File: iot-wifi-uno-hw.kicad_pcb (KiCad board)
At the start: 2 copper layers, 68.6 x 53.3 mm, 86 parts, among them CON1 BARREL_JACK, P1 CONN_01X08, P2 CONN_01X08, P3 CONN_01X06, P4 CONN_01X10, P5 CONN_01X04, Q1 Q_NPN_CBE, Q2 Q_NPN_CBE, U1 usb_mini_b, U2 BD00GA5WEFJ, U3 MCP16311-MNY, U4 CH340G, U5 ESP-12E, U6 MCP6001R, U7 MOSFET-P, X1 CRYSTAL_ABM3C

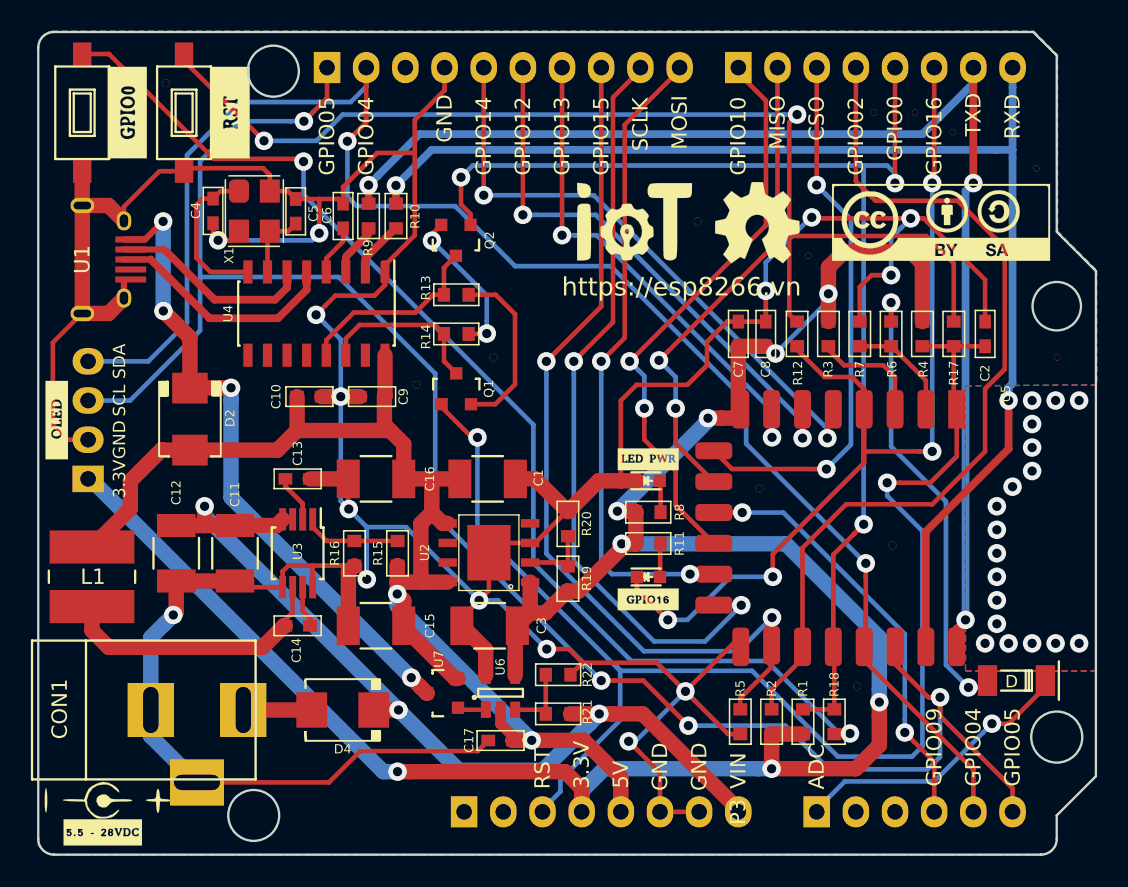
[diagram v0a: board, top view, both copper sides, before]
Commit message: Fix PCB diode zenner right
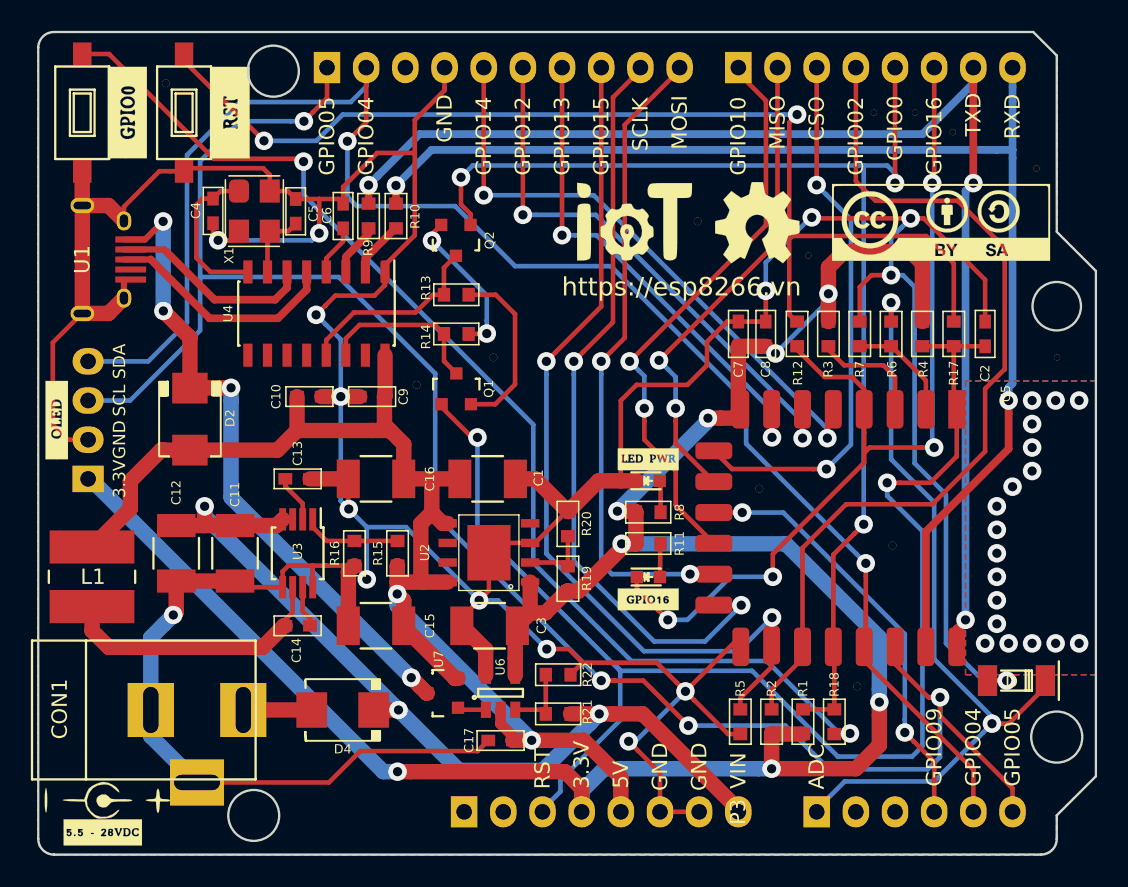
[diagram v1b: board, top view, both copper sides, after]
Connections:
- D pad 2: ADC_EX -> GND
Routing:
- net GND: track 293.4 -> 325.4 mm, vias 15 -> 16
- net ADC_EX: track 48.4 -> 49.9 mm, vias 3 -> 2
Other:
- net class Default: trace_width 0.5 -> 0.3
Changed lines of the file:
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@@
     (links 165)
     (no_connects 4)
-    (area 109.471337 58.578471 178.201339 112.068473)
+    (area 101.163667 55.951666 178.338002 114.228333)
     (thickness 1.6)
     (drawings 48)
-    (tracks 821)
+    (tracks 828)
     (zones 0)
     (modules 86)
@@
   )
   (setup
-    (last_trace_width 0.5)
+    (last_trace_width 0.3)
     (trace_clearance 0.1)
     (zone_clearance 0.5)
@@
     (mod_text_size 1 1)
     (mod_text_width 0.25)
-    (pad_size 0.4 0.4)
-    (pad_drill 0.4)
+    (pad_size 1.25 2)
+    (pad_drill 0)
     (pad_to_mask_clearance 0.2)
     (aux_axis_origin 0 0)
@@
   (net_class Default "This is the default net class."
     (clearance 0.1)
-    (trace_width 0.5)
+    (trace_width 0.3)
     (via_dia 1.2)
     (via_drill 0.6)
@@
       (net 9 ADC_EX))
     (pad 2 smd rect (at 1.875 0 180) (size 1.25 2) (layers F.Cu F.Paste F.Mask)
-      (net 9 ADC_EX))
+      (net 44 GND))
     (model "/home/trinhduc/Desktop/kicadlibrary/Untitled Folder/walter/smd_diode/sod80c.wrl"
       (at (xyz 0 0 0))
@@
   (via (at 157.124402 96.6216) (size 1.2) (drill 0.6) (layers F.Cu B.Cu) (net 8))
   (segment (start 157.1 97.82) (end 157.1 99.5162) (width 0.3) (layer F.Cu) (net 8) (status 30))
-  (segment (start 164.846 76.2) (end 164.846 85.5345) (width 0.3) (layer B.Cu) (net 9))
-  (segment (start 164.846 85.5345) (end 168.402 89.0905) (width 0.3) (layer B.Cu) (net 9))
-  (segment (start 168.402 89.0905) (end 168.402 99.695) (width 0.3) (layer B.Cu) (net 9))
-  (segment (start 168.402 99.695) (end 169.8625 101.1555) (width 0.3) (layer B.Cu) (net 9))
+  (segment (start 164.846 76.2) (end 164.846 86.36) (width 0.3) (layer B.Cu) (net 9))
+  (segment (start 164.846 86.36) (end 167.64 89.154) (width 0.3) (layer B.Cu) (net 9))
+  (segment (start 167.64 89.154) (end 167.64 99.314) (width 0.3) (layer B.Cu) (net 9))
+  (segment (start 167.64 99.314) (end 171.3865 103.0605) (width 0.3) (layer B.Cu) (net 9))
+  (segment (start 171.3865 103.0605) (end 171.3865 103.505) (width 0.3) (layer B.Cu) (net 9))
   (segment (start 160.02 109.22) (end 160.02 109.0676) (width 0.3) (layer B.Cu) (net 9))
   (segment (start 160.02 109.0676) (end 161.8361 107.2515) (width 0.3) (layer B.Cu) (net 9))
@@
   (segment (start 174.849 101.122) (end 174.849 100.711) (width 0.3) (layer F.Cu) (net 9))
   (via (at 171.3865 103.505) (size 1.2) (drill 0.6) (layers F.Cu B.Cu) (net 9))
-  (segment (start 169.8625 101.1555) (end 170.6545 101.1555) (width 0.3) (layer F.Cu) (net 9))
-  (segment (start 170.6545 101.1555) (end 171.099 100.711) (width 0.3) (layer F.Cu) (net 9))
-  (via (at 169.8625 101.1555) (size 1.2) (drill 0.6) (layers F.Cu B.Cu) (net 9))
   (segment (start 164.846 77.432001) (end 164.846 76.2) (width 0.3) (layer F.Cu) (net 9))
   (via (at 164.846 76.2) (size 1.2) (drill 0.6) (layers F.Cu B.Cu) (net 9))
@@
   (segment (start 118.999 60.5282) (end 124.1806 65.7098) (width 0.3) (layer F.Cu) (net 13))
   (via (at 124.1806 65.7098) (size 1.2) (drill 0.6) (layers F.Cu B.Cu) (net 13))
-  (segment (start 167.513 85.852) (end 167.513 68.453002) (width 0.3) (layer B.Cu) (net 14))
+  (segment (start 166.791466 85.598) (end 167.639994 85.598) (width 0.3) (layer F.Cu) (net 14))
+  (segment (start 163.4556 85.598) (end 166.791466 85.598) (width 0.3) (layer F.Cu) (net 14))
+  (segment (start 163.1 85.9536) (end 163.4556 85.598) (width 0.3) (layer F.Cu) (net 14))
+  (segment (start 167.513002 68.453) (end 167.513002 85.471008) (width 0.3) (layer B.Cu) (net 14))
+  (segment (start 167.513002 85.471008) (end 167.639994 85.598) (width 0.3) (layer B.Cu) (net 14))
+  (via (at 167.639994 85.598) (size 1.2) (drill 0.6) (layers F.Cu B.Cu) (net 14))
   (segment (start 167.64 68.326002) (end 167.513002 68.453) (width 0.3) (layer F.Cu) (net 14))
   (segment (start 167.64 60.96) (end 167.64 68.326002) (width 0.3) (layer F.Cu) (net 14))
-  (segment (start 167.513 68.453002) (end 167.513002 68.453) (width 0.3) (layer B.Cu) (net 14))
   (via (at 167.513002 68.453) (size 1.2) (drill 0.6) (layers F.Cu B.Cu) (net 14))
   (segment (start 157.1752 93.98) (end 154.432 93.98) (width 0.3) (layer B.Cu) (net 14))
@@
   (segment (start 148.3614 93.9927) (end 148.3614 94.7674) (width 0.3) (layer F.Cu) (net 14))
   (via (at 150.368 96.774) (size 1.2) (drill 0.6) (layers F.Cu B.Cu) (net 14))
-  (segment (start 166.664472 85.852) (end 167.513 85.852) (width 0.3) (layer F.Cu) (net 14))
-  (segment (start 163.2016 85.852) (end 166.664472 85.852) (width 0.3) (layer F.Cu) (net 14))
-  (segment (start 163.1 85.9536) (end 163.2016 85.852) (width 0.3) (layer F.Cu) (net 14))
-  (via (at 167.513 85.852) (size 1.2) (drill 0.6) (layers F.Cu B.Cu) (net 14))
   (segment (start 163.1 83.82) (end 163.1 81.82) (width 0.3) (layer F.Cu) (net 14))
   (segment (start 163.1 81.82) (end 162.306 81.026) (width 0.3) (layer F.Cu) (net 14))
@@
   (segment (start 125.6792 75.2348) (end 124.9045 76.0095) (width 0.5) (layer F.Cu) (net 43))
   (segment (start 124.9045 76.0095) (end 120.9675 76.0095) (width 0.5) (layer F.Cu) (net 43))
+  (segment (start 164.846 74.422006) (end 165.608006 74.422006) (width 0.3) (layer B.Cu) (net 44))
+  (segment (start 165.608006 74.422006) (end 166.37 75.184) (width 0.3) (layer B.Cu) (net 44))
+  (segment (start 166.37 75.184) (end 166.37 86.614) (width 0.3) (layer B.Cu) (net 44))
+  (segment (start 166.37 86.614) (end 168.402 88.646) (width 0.3) (layer B.Cu) (net 44))
+  (segment (start 168.402 88.646) (end 168.402 98.298) (width 0.3) (layer B.Cu) (net 44))
+  (segment (start 168.402 98.298) (end 170.815 100.711) (width 0.3) (layer B.Cu) (net 44))
+  (segment (start 170.815 100.711) (end 172.339 100.711) (width 0.3) (layer B.Cu) (net 44))
+  (segment (start 172.339 100.711) (end 171.099 100.711) (width 0.3) (layer F.Cu) (net 44))
+  (via (at 172.339 100.711) (size 1.2) (drill 0.6) (layers F.Cu B.Cu) (net 44))
   (segment (start 156.718 75.437994) (end 156.718 73.5965) (width 0.3) (layer B.Cu) (net 44))
   (segment (start 156.718 73.5965) (end 159.639 70.6755) (width 0.3) (layer B.Cu) (net 44))
@@
   (segment (start 126.5682 66.8782) (end 126.746 67.056) (width 0.3) (layer F.Cu) (net 49))
   (via (at 126.746 67.056) (size 1.2) (drill 0.6) (layers F.Cu B.Cu) (net 49))
-  (zone (net 44) (net_name GND) (layer B.Cu) (hatch edge 0.508)
+  (zone (net 44) (net_name GND) (layer F.Cu) (hatch edge 0.508)
     (connect_pads (clearance 0.4))
     (min_thickness 0.4)
@@
     (polygon
       (pts
-        (xy 110.4265 58.6105) (xy 174.117 58.6105) (xy 175.641 60.1345) (xy 175.641 71.5645) (xy 178.181 74.1045)
-        (xy 178.181 81.534) (xy 169.672 81.5975) (xy 169.672 100.076) (xy 178.1175 100.076) (xy 178.1175 106.934)
-        (xy 175.5775 109.474) (xy 175.5775 111.252) (xy 175.387 111.633) (xy 174.9425 111.9505) (xy 174.5615 112.014)
-        (xy 110.363 112.014) (xy 109.9185 111.8235) (xy 109.601 111.379) (xy 109.5375 111.0615) (xy 109.5375 59.4995)
-        (xy 109.601 59.2455) (xy 109.7915 58.9915) (xy 109.982 58.801)
+        (xy 110.3884 58.674) (xy 174.0916 58.674) (xy 175.6156 60.198) (xy 175.6156 71.628) (xy 178.1556 74.168)
+        (xy 178.1556 81.28) (xy 169.672 81.28) (xy 169.672 100.33) (xy 178.1556 100.33) (xy 178.1556 106.8832)
+        (xy 175.6156 109.4232) (xy 175.6156 111.1504) (xy 175.4632 111.506) (xy 175.2092 111.76) (xy 174.752 111.9632)
+        (xy 110.5916 112.014) (xy 110.236 111.9632) (xy 109.8804 111.76) (xy 109.6264 111.4552) (xy 109.5248 110.9472)
+        (xy 109.5248 59.436) (xy 109.8296 58.928) (xy 110.0328 58.7756)
       )
     )
   )
-  (zone (net 44) (net_name GND) (layer F.Cu) (hatch edge 0.508)
+  (zone (net 44) (net_name GND) (layer B.Cu) (hatch edge 0.508)
     (connect_pads (clearance 0.4))
     (min_thickness 0.4)
@@
     (polygon
       (pts
-        (xy 110.4265 58.6105) (xy 174.0535 58.6105) (xy 175.5775 60.1345) (xy 175.641 71.5645) (xy 178.1175 74.1045)
-        (xy 178.181 81.534) (xy 169.672 81.5975) (xy 169.672 100.076) (xy 178.1175 100.076) (xy 178.1175 106.8705)
-        (xy 175.5775 109.474) (xy 175.5775 111.252) (xy 175.387 111.633) (xy 175.1965 111.8235) (xy 174.752 112.014)
-        (xy 174.371 112.014) (xy 110.4265 112.014) (xy 109.9185 111.76) (xy 109.5375 111.4425) (xy 109.5375 110.8075)
-        (xy 109.5375 59.563) (xy 109.6645 59.182) (xy 109.7915 58.928) (xy 110.1725 58.674)
+        (xy 110.4392 58.674) (xy 174.0916 58.674) (xy 175.6156 60.198) (xy 175.6156 71.628) (xy 178.1556 74.168)
+        (xy 178.1556 81.28) (xy 169.672 81.28) (xy 169.672 100.33) (xy 178.1556 100.33) (xy 178.1556 106.8832)
+        (xy 175.5648 109.4232) (xy 175.5648 111.1504) (xy 175.4124 111.5568) (xy 175.1076 111.8108) (xy 174.752 111.9632)
+        (xy 174.4472 112.014) (xy 110.4392 112.014) (xy 109.8804 111.76) (xy 109.6264 111.4552) (xy 109.5248 111.0488)
+        (xy 109.5248 59.436) (xy 109.728 59.0804) (xy 109.982 58.8264)
       )
     )

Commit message: update README file
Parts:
- removed C16: 10uF/25V, Capacitors_SMD:C_1210_HandSoldering
- removed C17: 100nF, ESP8266:C_0603
- removed D: SOD-80, ESP8266:SOD-80
- removed the G*** at (156.1, 71.1)
- removed GPIO0: GPIO0, ESP8266:Tact_Switch_TS6X3.6
- removed the REF** at (175.0, 79.8)
- removed the REF** at (164.3, 91.9)
- removed the REF** at (155.7, 88.3)
- removed the REF** at (133.5, 81.5)
- removed the REF** at (117.2, 62.0)
- removed the REF** at (173.7, 67.5)
- removed the REF** at (151.7, 70.9)
- removed the REF** at (162.1, 101.1)
- removed the REF** at (158.9, 73.2)
- removed the REF** at (168.2, 65.2)
- removed the REF** at (165.8, 63.9)
- removed the REF** at (163.1, 63.9)
- removed the REF** at (138.5, 79.8)
- added D5: ZENER_3.3V, ESP8266:SOD-80, F.Cu at (164.1, 102.6)
- added G***: LOGO, ESP8266:logo_openhardware_5x5mm, F.Cu at (153.4, 71.6)
- added GPIO1: GPIO0, ESP8266:Tact_Switch_TS6X3.6, F.Cu at (112.0, 64.0)
- added REF**: gnd_via, ESP8266:gnd_via, F.Cu at (112.3, 63.0)
- added REF**: gnd_via, ESP8266:gnd_via, F.Cu at (136.9, 85.5)
- added REF**: gnd_via, ESP8266:gnd_via, F.Cu at (133.1, 78.7)
- added REF**: gnd_via, ESP8266:gnd_via, F.Cu at (149.2, 68.6)
- added REF**: gnd_via, ESP8266:gnd_via, F.Cu at (139.2, 65.3)
- added REF**: gnd_via, ESP8266:gnd_via, F.Cu at (171.2, 67.9)
- added REF**: gnd_via, ESP8266:gnd_via, F.Cu at (164.3, 68.2)
- added REF**: gnd_via, ESP8266:gnd_via, F.Cu at (168.2, 106.8)
- added REF**: gnd_via, ESP8266:gnd_via, F.Cu at (119.4, 78.2)
- added REF**: gnd_via, ESP8266:gnd_via, F.Cu at (128.3, 89.7)
- added REF**: gnd_via, ESP8266:gnd_via, F.Cu at (143.3, 76.7)
- added REF**: gnd_via, ESP8266:gnd_via, F.Cu at (174.6, 79.5)
- added REF**: gnd_via, ESP8266:gnd_via, F.Cu at (141.6, 66.3)
- added REF**: gnd_via, ESP8266:gnd_via, F.Cu at (156.6, 68.1)
- added REF**: gnd_via, ESP8266:gnd_via, F.Cu at (152.4, 59.3)
- added REF**: gnd_via, ESP8266:gnd_via, F.Cu at (170.8, 103.9)
- C1: value 1uF/25V -> 22pF; footprint Capacitors_SMD:C_1210_HandSoldering -> ESP8266:C_0603
- C10: value 100nF -> 10uF/25V; footprint ESP8266:C_0603 -> ESP8266:C_1210
- C11: value 10uF/50V -> 10uF/25V; footprint Capacitors_SMD:C_1210_HandSoldering -> ESP8266:C_1210
- C12: value 10uF/50V -> 100nF; footprint Capacitors_SMD:C_1210_HandSoldering -> ESP8266:C_0603
- C13: value 1uF -> 1uF/25V; footprint ESP8266:C_0603 -> ESP8266:C_1210
- C15: value 10uF/25V -> 1uF/25V; footprint Capacitors_SMD:C_1210_HandSoldering -> ESP8266:C_0603
- C2: value 470pF -> 22pF
- C3: value 1uF/25V -> 10uF/50V; footprint Capacitors_SMD:C_1210_HandSoldering -> ESP8266:C_1210
- C4: value 8pF -> 10uF/50V; footprint ESP8266:C_0603 -> ESP8266:C_1210
- C5: value 8pF -> 470pF
- C7: value 10uF/25v -> 1uF
- C9: value 10uF -> 100nF
- D1: value L_PWR -> SS24; footprint LEDs:LED_0603 -> ESP8266:do214aa-g
- D2: value ss24 -> LED_Blue; footprint ESP8266:do214aa -> LEDs:LED_0603
- D3: value LED_Blue -> SS24; footprint LEDs:LED_0603 -> ESP8266:do214aa-g
- D4: value D -> L_PWR; footprint ESP8266:do214aa-g -> LEDs:LED_0603
- L1: value 22uF -> 22uH
- Q1, Q2: value Q_NPN_CBE -> MMBT8050LT1G
- R10, R11: value 470R -> 10K
- R12: value 0R -> 470R
- R13: value 10K -> 0R
- R14: value 10K -> 470R
- R15: value 52.5K -> 220k/1%
- R16: value 10k -> 100k/1%
- R18, R9: value 470R -> 10k
- R19: value 3K/1% -> 10k
- R20: value 1K/1% -> 3K/1%
- R21: value 10k -> 1K/1%
- R22: value 10k -> 470R
- R6: value 220k/1% -> 470R
- R7: value 100k/1% -> 470R
- R8: value 470R -> 52.5K
- U2: value BD00GA5WEFJ -> MCP16311-MNY; footprint ESP8266:HTSOP-J8 -> Housings_SSOP:MSOP-8_3x3mm_Pitch0.65mm
- U3: value MCP16311-MNY -> CH340G; footprint Housings_SSOP:MSOP-8_3x3mm_Pitch0.65mm -> Housings_SOIC:SOIC-16_3.9x9.9mm_Pitch1.27mm
- U4: value CH340G -> ESP-12E; footprint Housings_SOIC:SOIC-16_3.9x9.9mm_Pitch1.27mm -> ESP8266:ESP-12F
- U5: value ESP-12E -> MCP6001R; footprint ESP8266:ESP-12F -> TO_SOT_Packages_SMD:SOT-23-5
- U6: value MCP6001R -> BD00GA5WEFJ; footprint TO_SOT_Packages_SMD:SOT-23-5 -> HTSOP-J8
- U7: value MOSFET-P -> IRLM6402
- moved C5 45.3 mm to (170.9, 77.5)
- moved C2 44.6 mm to (127.0, 70.6)
- moved U4 42.0 mm to (169.2, 83.1)
- moved R16 37.0 mm to (163.8, 77.5)
- moved R15 36.0 mm to (165.6, 77.5)
- moved R6 34.6 mm to (131.1, 70.6), turned to 270 degrees
- moved U5 33.7 mm to (140.3, 101.3)
- moved D3 31.6 mm to (118.6, 85.9), turned to 90 degrees
- moved R14 30.7 mm to (167.4, 77.5), turned to 90 degrees
- moved R7 30.7 mm to (133.1, 70.6)
- moved D2 30.2 mm to (148.1, 93.1), turned to 0 degrees
- moved R18 26.6 mm to (134.6, 101.3)
- moved R17 25.5 mm to (161.2, 102.6), turned to 270 degrees
- moved D1 25.2 mm to (128.4, 102.1), turned to 270 degrees
- moved C7 24.9 mm to (131.0, 85.2), turned to 180 degrees
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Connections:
- C1 pad 1: +5V -> XO
- C11 pad 1: Vin -> +5V
- C12 pad 1: Vin -> +5V
- C13 pad 1: Net-(C13-Pad1) -> +5V
- C14 pad 1: Net-(C14-Pad1) -> +5V
- C14 pad 2: Net-(C14-Pad2) -> GND
- C15 pad 1: +5V -> +3V3
- C2 pad 1: REST -> XI
- C3 pad 1: +3V3 -> Vin
- C4 pad 1: XO -> Vin
- C5 pad 1: XI -> REST
- C7 pad 1: +3V3 -> Net-(C7-Pad1)
- C9 pad 1: +5V -> Net-(C9-Pad1)
- C9 pad 2: GND -> Net-(C9-Pad2)
- D1 pad 1: GND -> Vin
- D1 pad 2: Net-(D1-Pad2) -> Net-(CON1-Pad1)
- D2 pad 1: +5V -> GPIO16
- D2 pad 2: VCC -> Net-(D2-Pad2)
- D3 pad 1: GPIO16 -> +5V
- D3 pad 2: Net-(D3-Pad2) -> VCC
- D4 pad 1: Vin -> GND
- D4 pad 2: Net-(CON1-Pad1) -> Net-(D4-Pad2)
- L1 pad 1: Net-(C14-Pad2) -> Net-(C9-Pad2)
- R10 pad 1: RXD -> Net-(Q2-Pad3)
- R10 pad 2: Net-(R10-Pad2) -> Net-(Q1-Pad2)
- R11 pad 1: +3V3 -> Net-(Q1-Pad3)
- R11 pad 2: Net-(D3-Pad2) -> Net-(Q2-Pad2)
- R12 pad 1: GPIO16 -> +3V3
- R12 pad 2: Net-(R12-Pad2) -> Net-(D2-Pad2)
- R13 pad 1: Net-(Q2-Pad3) -> GPIO16
- R13 pad 2: Net-(Q1-Pad2) -> Net-(R13-Pad2)
- R14 pad 1: Net-(Q1-Pad3) -> REST
- R14 pad 2: Net-(Q2-Pad2) -> Net-(R13-Pad2)
- R15 pad 1: +5V -> ADC
- R15 pad 2: Net-(R15-Pad2) -> ADC_EX
- R16 pad 1: Net-(R15-Pad2) -> GND
- R16 pad 2: GND -> ADC
- R17 pad 1: REST -> GPIO0
- R17 pad 2: Net-(R12-Pad2) -> Net-(GPIO1-Pad1)
- R18 pad 1: GPIO0 -> Net-(R18-Pad1)
- R18 pad 2: Net-(GPIO0-Pad1) -> Vin
- R19 pad 1: +3V3 -> GND
- R19 pad 2: Net-(R19-Pad2) -> Net-(R18-Pad1)
- R20 pad 1: Net-(R19-Pad2) -> +3V3
- R20 pad 2: GND -> Net-(R20-Pad2)
- R21 pad 1: Net-(R21-Pad1) -> Net-(R20-Pad2)
- R21 pad 2: Vin -> GND
- R22 pad 1: GND -> +3V3
- R22 pad 2: Net-(R21-Pad1) -> Net-(D4-Pad2)
- R6 pad 1: ADC -> TXD
- R6 pad 2: ADC_EX -> Net-(R6-Pad2)
- R7 pad 1: GND -> RXD
- R7 pad 2: ADC -> Net-(R7-Pad2)
- R8 pad 1: +3V3 -> +5V
- R8 pad 2: Net-(D1-Pad2) -> Net-(R8-Pad2)
- R9 pad 1: TXD -> Net-(R8-Pad2)
- R9 pad 2: Net-(R9-Pad2) -> GND
- RST1 pad 1: Net-(R12-Pad2) -> Net-(R13-Pad2)
- U2 pad 1: +3V3 -> Net-(R8-Pad2)
- U2 pad 2: Net-(R19-Pad2) -> Net-(C7-Pad1)
- U2 pad 3: GND -> Vin
- U2 pad 4: (no net) -> Vin
- U2 pad 5: +5V -> GND
- U2 pad 6: (no net) -> Net-(C9-Pad2)
- U2 pad 7: (no net) -> Net-(C9-Pad1)
- U2 pad 8: +5V -> GND
- U3 pad 1: Net-(R15-Pad2) -> GND
- U3 pad 2: Net-(C13-Pad1) -> Net-(R7-Pad2)
- U3 pad 3: Vin -> Net-(R6-Pad2)
- U3 pad 4: Vin -> Net-(C6-Pad1)
- U3 pad 5: GND -> D+
- U3 pad 6: Net-(C14-Pad2) -> D-
- U3 pad 7: Net-(C14-Pad1) -> XI
- U3 pad 8: GND -> XO
- U4 pad 1: GND -> REST
- U4 pad 10: (no net) -> MISO
- U4 pad 11: (no net) -> GPIO09
- U4 pad 12: (no net) -> GPIO10
- U4 pad 13: Net-(Q2-Pad3) -> MOSI
- U4 pad 14: Net-(Q1-Pad3) -> SCLK
- U4 pad 15: (no net) -> GND
- U4 pad 16: +5V -> GPIO15
- U4 pad 2: Net-(R10-Pad2) -> ADC
- U4 pad 3: Net-(R9-Pad2) -> EN
- U4 pad 4: Net-(C6-Pad1) -> GPIO16
- U4 pad 5: D+ -> GPIO14
- U4 pad 6: D- -> GPIO12
- U4 pad 7: XI -> GPIO13
- U4 pad 8: XO -> +3V3
- U4 pad 9: (no net) -> CSO
- U5 pad 1: REST -> Net-(U5-Pad1)
- U5 pad 2: ADC -> +5V
- U5 pad 3: EN -> Net-(R18-Pad1)
- U5 pad 4: GPIO16 -> +3V3
- U5 pad 5: GPIO14 -> GND
- U6 pad 1: Net-(U6-Pad1) -> +3V3
- U6 pad 2: +5V -> Net-(R20-Pad2)
- U6 pad 3: Net-(R21-Pad1) -> GND
- U6 pad 4: +3V3 -> (no net)
- U6 pad 5: GND -> +5V
- U7 pad 1: Net-(U6-Pad1) -> Net-(U5-Pad1)
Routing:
- net Net-(R13-Pad2): track 0.00 -> 89.9 mm, vias 0 -> 5
- net Net-(GPIO1-Pad1): track 0.00 -> 78.3 mm, vias 0 -> 2
- net Net-(GPIO0-Pad1): track 75.6 -> 0.00 mm, vias 2 -> 0
- net Net-(R12-Pad2): track 72.1 -> 0.00 mm, vias 2 -> 0
- net Net-(D2-Pad2): track 0.00 -> 28.3 mm, vias 0 -> 2
- net GPIO4: track 106.0 -> 133.0 mm, vias 2 -> 3
- net Net-(C9-Pad2): track 0.00 -> 25.6 mm
- net GND: track 325.4 -> 300.3 mm, vias 16 -> 7
- net +5V: track 84.4 -> 105.5 mm, vias 2 -> 5
- net VCC: track 42.3 -> 62.4 mm, vias 4 -> 3
- net REST: track 90.6 -> 108.7 mm, vias 2 -> 1
- net Net-(C14-Pad2): track 17.8 -> 0.00 mm
- net GPIO14: track 39.7 -> 56.7 mm
- net GPIO2: track 60.0 -> 45.2 mm, vias 0 -> 2
- net GPIO13: track 32.1 -> 46.1 mm
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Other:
- net class Default: clearance 0.1 -> 0.254; trace_width 0.3 -> 0.4; via_dia 1.2 -> 1.1
- rule trace_clearance: 0.1 -> 0.254
- board text added: "SCL/GPIO5"
- board text added: "SDA/GPIO4"
- board text removed: "SCL"
- board text removed: "SDA"
